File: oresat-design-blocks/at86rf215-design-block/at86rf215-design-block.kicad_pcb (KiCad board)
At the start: 2 copper layers, 1 part, among them U2 AT86RF215-ZU

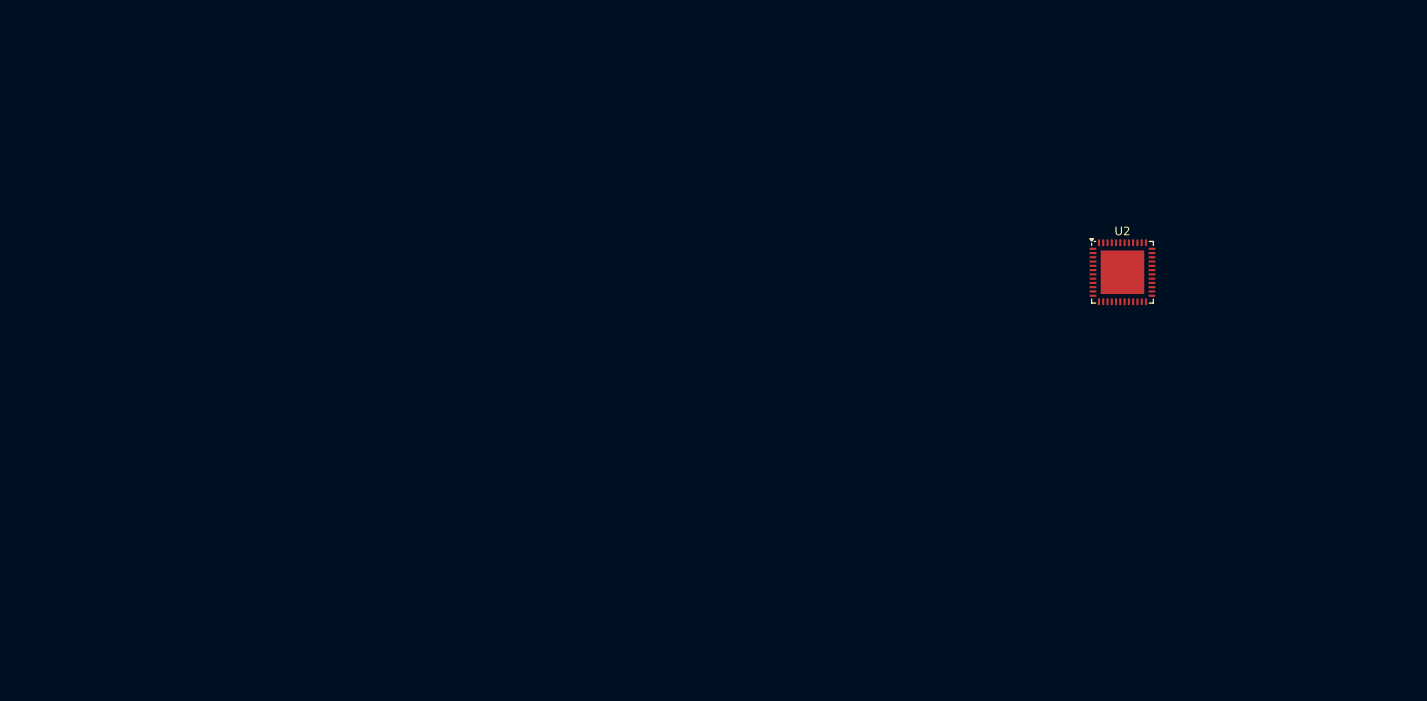
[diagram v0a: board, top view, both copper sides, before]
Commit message: added initial footprints and oreganized schematic. Started PCB
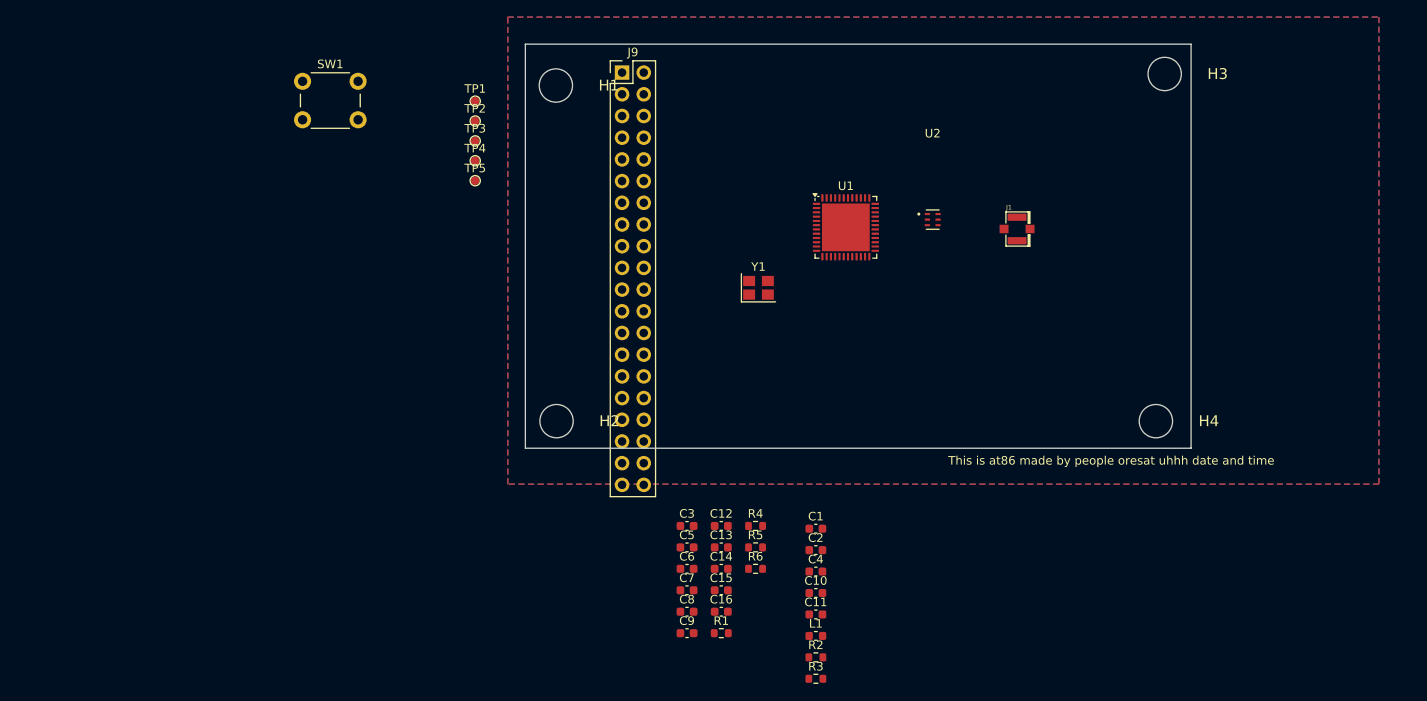
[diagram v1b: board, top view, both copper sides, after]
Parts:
- added C1: 1.8p, Capacitor_SMD:C_0603_1608Metric, F.Cu at (118.5, 113.1)
- added C10: 1.2p, Capacitor_SMD:C_0603_1608Metric, F.Cu at (118.5, 120.6)
- added C11: 1.2p, Capacitor_SMD:C_0603_1608Metric, F.Cu at (118.5, 123.1)
- added C12: 100 nF, Capacitor_SMD:C_0603_1608Metric, F.Cu at (107.4, 112.8)
- added C13: 100 nF, Capacitor_SMD:C_0603_1608Metric, F.Cu at (107.4, 115.3)
- added C14: 100 nF, Capacitor_SMD:C_0603_1608Metric, F.Cu at (107.4, 117.8)
- added C15: 100 nF, Capacitor_SMD:C_0603_1608Metric, F.Cu at (107.4, 120.3)
- added C16: 100 nF, Capacitor_SMD:C_0603_1608Metric, F.Cu at (107.4, 122.8)
- added C2: 1.8p, Capacitor_SMD:C_0603_1608Metric, F.Cu at (118.5, 115.6)
- added C3: 100n, Capacitor_SMD:C_0603_1608Metric, F.Cu at (103.4, 112.8)
- added C4: 0.8p, Capacitor_SMD:C_0603_1608Metric, F.Cu at (118.5, 118.1)
- added C5: 4.7n, Capacitor_SMD:C_0603_1608Metric, F.Cu at (103.4, 115.3)
- added C6: 2.2p, Capacitor_SMD:C_0603_1608Metric, F.Cu at (103.4, 117.8)
- added C7: 100 nF, Capacitor_SMD:C_0603_1608Metric, F.Cu at (103.4, 120.3)
- added C8: 100 nF, Capacitor_SMD:C_0603_1608Metric, F.Cu at (103.4, 122.8)
- added C9: 100 nF, Capacitor_SMD:C_0603_1608Metric, F.Cu at (103.4, 125.3)
- added H1: MountingHole, oresat-misc:M2-Press-Fit-Nut, F.Cu at (88.0, 61.2)
- added H2: MountingHole, oresat-misc:M2-Press-Fit-Nut, F.Cu at (88.1, 100.5)
- added H3: MountingHole, oresat-misc:M2-Press-Fit-Nut, F.Cu at (159.3, 59.9)
- added H4: MountingHole, oresat-misc:M2-Press-Fit-Nut, F.Cu at (158.3, 100.5)
- added J1: Conn_Coaxial, oresat-connectors:J-U.FL, F.Cu at (142.0, 78.0)
- added J9: Conn_02x20_Odd_Even, Connector_PinHeader_2.54mm:PinHeader_2x20_P2.54mm_Vertical, F.Cu at (95.8, 59.7)
- added L1: 5.6n, Inductor_SMD:L_0603_1608Metric, F.Cu at (118.5, 125.7)
- added R1: 100k, Resistor_SMD:R_0603_1608Metric, F.Cu at (107.4, 125.3)
- added R2: 0, Resistor_SMD:R_0603_1608Metric, F.Cu at (118.5, 128.2)
- added R3: 220, Resistor_SMD:R_0603_1608Metric, F.Cu at (118.5, 130.7)
- added R4: 39, Resistor_SMD:R_0603_1608Metric, F.Cu at (111.4, 112.8)
- added R5: 220, Resistor_SMD:R_0603_1608Metric, F.Cu at (111.4, 115.3)
- added R6: 100k, Resistor_SMD:R_0603_1608Metric, F.Cu at (111.4, 117.8)
- added SW1: RESET, Button_Switch_THT:SW_PUSH_6mm, F.Cu at (58.4, 60.7)
- added TP1: ~, oresat-misc:TestPoint_Pad_D1.0mm, F.Cu at (78.6, 63.1)
- added TP2: ~, oresat-misc:TestPoint_Pad_D1.0mm, F.Cu at (78.6, 65.4)
- added TP3: ~, oresat-misc:TestPoint_Pad_D1.0mm, F.Cu at (78.6, 67.7)
- added TP4: ~, oresat-misc:TestPoint_Pad_D1.0mm, F.Cu at (78.6, 70.0)
- added TP5: ~, oresat-misc:TestPoint_Pad_D1.0mm, F.Cu at (78.6, 72.4)
- added U1: AT86RF215, Package_DFN_QFN:QFN-48-1EP_7x7mm_P0.5mm_EP5.6x5.6mm, F.Cu at (122.0, 77.8)
- added Y1: TXETACSANF-26.000000, Crystal:Crystal_SMD_Abracon_ABM8AIG-4Pin_3.2x2.5mm, F.Cu at (111.8, 84.9)
- U2: value AT86RF215-ZU -> 2450FB15A050E; footprint Package_DFN_QFN:QFN-48-1EP_7x7mm_P0.5mm_EP5.1x5.1mm -> oresat-passives:2450FB15A050E_JOT
- moved U2 23.1 mm to (132.2, 76.9)
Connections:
- U2 pad 1: FEA24 -> Net-(U2-IN)
- U2 pad 2: FEB24 -> GND
- U2 pad 3: GNDA -> Net-(U2-OUT1)
- U2 pad 4: RFP24 -> Net-(U2-OUT2)
- U2 pad 5: RFN24 -> GND
- U2 pad 6: GNDA -> unconnected-(U2-NC-Pad6)
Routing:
- added copper zone on B.Cu, net GND
- added copper zone on F.Cu, net GND
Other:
- board outline added: 77.9 x 47.3 mm
- board text added: "This is at86 made by people oresat uhhh date and time"

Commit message: added initial 436.5mhz circuit
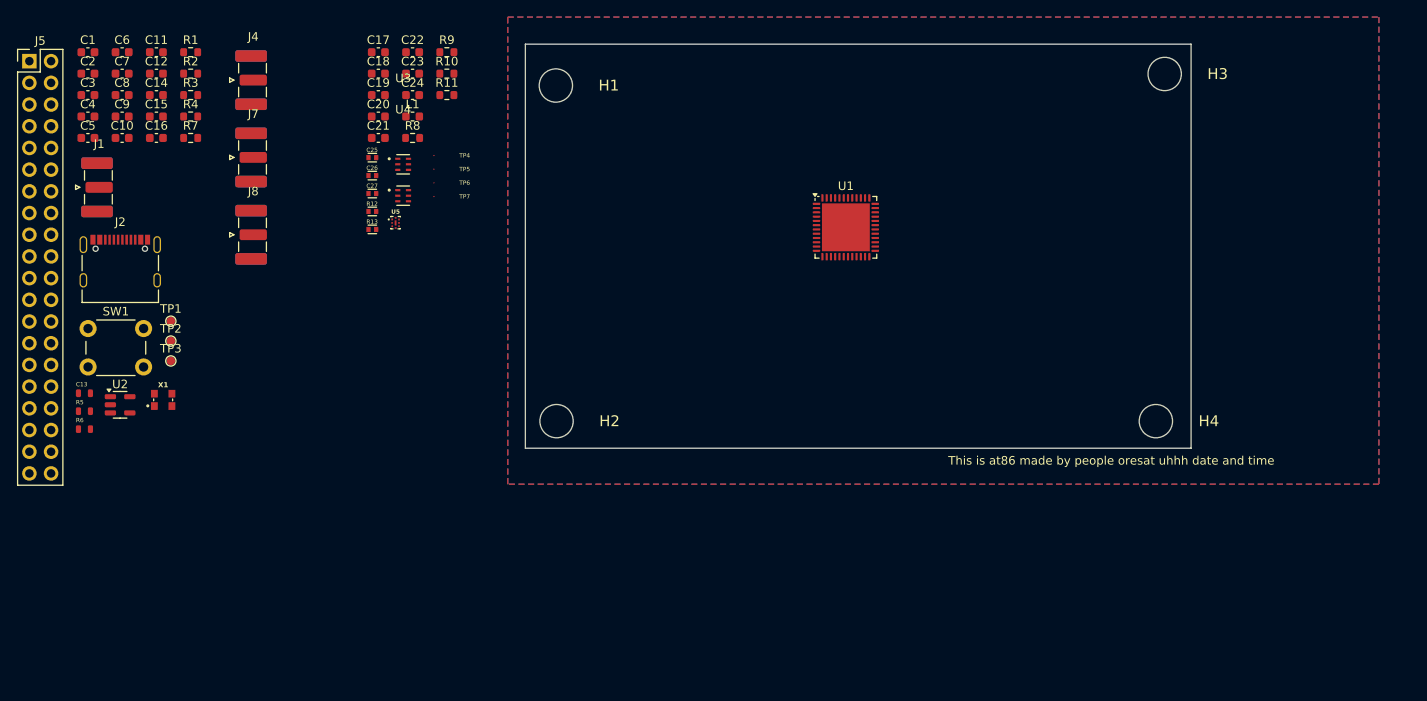
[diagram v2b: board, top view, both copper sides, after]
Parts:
- removed J9: Conn_02x20_Odd_Even, Connector_PinHeader_2.54mm:PinHeader_2x20_P2.54mm_Vertical
- removed Y1: TXETACSANF-26.000000, Crystal:Crystal_SMD_Abracon_ABM8AIG-4Pin_3.2x2.5mm
- added C17: 1.8p, Capacitor_SMD:C_0603_1608Metric, F.Cu at (67.3, 57.3)
- added C18: 1.8p, Capacitor_SMD:C_0603_1608Metric, F.Cu at (67.3, 59.8)
- added C19: 0.8p, Capacitor_SMD:C_0603_1608Metric, F.Cu at (67.3, 62.3)
- added C20: 15p, Capacitor_SMD:C_0603_1608Metric, F.Cu at (67.3, 64.8)
- added C21: 1.2p, Capacitor_SMD:C_0603_1608Metric, F.Cu at (67.3, 67.4)
- added C22: 2.2p, Capacitor_SMD:C_0603_1608Metric, F.Cu at (71.3, 57.3)
- added C23: 1.2p, Capacitor_SMD:C_0603_1608Metric, F.Cu at (71.3, 59.8)
- added C24: 2.2p, Capacitor_SMD:C_0603_1608Metric, F.Cu at (71.3, 62.3)
- added C25: 100p, oresat-passives:0402-C, F.Cu at (66.6, 69.7)
- added C26: 2200p, oresat-passives:0402-C, F.Cu at (66.6, 71.8)
- added C27: 100p, oresat-passives:0402-C, F.Cu at (66.6, 73.9)
- added J2: USB4105-GF-A, Connector_USB:USB_C_Receptacle_Palconn_UTC16-G, F.Cu at (37.0, 81.8)
- added J4: SMA, Connector_Coaxial:SMA_Samtec_SMA-J-P-H-ST-EM1_EdgeMount, F.Cu at (52.6, 60.6)
- added J5: Conn_02x20_Odd_Even, Connector_PinHeader_2.54mm:PinHeader_2x20_P2.54mm_Vertical, F.Cu at (26.4, 58.4)
- added J7: SMA, Connector_Coaxial:SMA_Samtec_SMA-J-P-H-ST-EM1_EdgeMount, F.Cu at (52.6, 69.6)
- added J8: SMA, Connector_Coaxial:SMA_Samtec_SMA-J-P-H-ST-EM1_EdgeMount, F.Cu at (52.6, 78.7)
- added R10: 10k, Resistor_SMD:R_0603_1608Metric, F.Cu at (75.3, 59.8)
- added R11: 10k, Resistor_SMD:R_0603_1608Metric, F.Cu at (75.3, 62.3)
- added R12: 10k, oresat-passives:0402-C, F.Cu at (66.6, 76.0)
- added R13: 5.62k, oresat-passives:0402-C, F.Cu at (66.6, 78.1)
- added R7: 100k, Resistor_SMD:R_0603_1608Metric, F.Cu at (45.3, 67.4)
- added R8: 0, Resistor_SMD:R_0603_1608Metric, F.Cu at (71.3, 67.4)
- added R9: 0, Resistor_SMD:R_0603_1608Metric, F.Cu at (75.3, 57.3)
- added TP6: ~, oresat-misc:TestPoint_RF_Probe, F.Cu at (73.8, 72.6)
- added TP7: ~, oresat-misc:TestPoint_RF_Probe, F.Cu at (73.8, 74.2)
- added U3: 2450FB15A050E, oresat-passives:2450FB15A050E_JOT, F.Cu at (70.2, 70.4)
- added U4: NCS2-62+, oresat-passives:2450FB15A050E_JOT, F.Cu at (70.2, 74.1)
- added U5: QPC1022, oresat-ics:QPC1022, F.Cu at (69.3, 77.3)
- added X1: TXETALSANF-26.000000, oresat-ics:X_TCXO_SMD_Taitien_2.5x2.0mm, F.Cu at (42.1, 98.0)
- C1: value 1.8p -> 100n
- C10, C11: value 1.2p -> 100 nF
- C13: value 100 nF -> 100n; footprint Capacitor_SMD:C_0603_1608Metric -> oresat-passives:0603-C-NOSILK
- C14: value 100 nF -> 4.7u
- C15: value 100 nF -> 10n
- C16: value 100 nF -> 1u
- C2: value 1.8p -> 4.7n
- C3: value 100n -> 1n
- C4: value 0.8p -> 2.2p
- C5: value 4.7n -> 100 nF
- C6: value 2.2p -> 100 nF
- J1: value Conn_Coaxial -> SMA; footprint oresat-connectors:J-U.FL -> Connector_Coaxial:SMA_Samtec_SMA-J-P-H-ST-EM1_EdgeMount
- R2: value 0 -> 39
- R4: value 39 -> 100k
- R5: value 220 -> 5.1k; footprint Resistor_SMD:R_0603_1608Metric -> oresat-passives:0603-C-NOSILK
- R6: value 100k -> 5.1k; footprint Resistor_SMD:R_0603_1608Metric -> oresat-passives:0603-C-NOSILK
- TP4, TP5: footprint oresat-misc:TestPoint_Pad_D1.0mm -> oresat-misc:TestPoint_RF_Probe
- U2: value 2450FB15A050E -> LP2985AIM5-1.8_NOPB; footprint oresat-passives:2450FB15A050E_JOT -> Package_TO_SOT_SMD:SOT-23-5
- moved J1 107.6 mm to (34.6, 73.1)
- moved C1 101.8 mm to (33.3, 57.3)
- moved C2 101.8 mm to (33.3, 59.8)
- moved C11 101.4 mm to (41.3, 57.3)
- moved C4 100.5 mm to (33.3, 64.8)
- moved R2 100.1 mm to (45.3, 59.8)
- moved R3 100.1 mm to (45.3, 62.3)
- moved U2 97.6 mm to (37.0, 98.6)
- moved C10 97.1 mm to (37.3, 67.4)
- moved R1 92.1 mm to (45.3, 57.3)
- moved C7 89.6 mm to (37.3, 59.8)
- moved C9 89.6 mm to (37.3, 64.8)
- moved C6 89.6 mm to (37.3, 57.3)
- moved C8 89.6 mm to (37.3, 62.3)
- moved C3 86.4 mm to (33.3, 62.3)
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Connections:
- C1 pad 1: Net-(U2-OUT1) -> GND
- C1 pad 2: RFN24 -> +3V3
- C10 pad 1: Net-(C10-Pad1) -> Net-(U1-AVDD0)
- C11 pad 1: Net-(J1-In) -> +3V3
- C12 pad 1: +3V3 -> Net-(U1-AVDD1)
- C13 pad 1: +3V3 -> GND
- C13 pad 2: GND -> Net-(J2-SHIELD)
- C14 pad 1: +3V3 -> 5V
- C15 pad 1: +3V3 -> Net-(U2-BYPASS)
- C16 pad 1: +3V3 -> 3.3V
- C2 pad 1: RFP24 -> ~{RSTN}
- C2 pad 2: Net-(U2-OUT2) -> GND
- C3 pad 1: GND -> Net-(U1-TXCO)
- C3 pad 2: +3V3 -> Net-(X1-OUT)
- C4 pad 1: Net-(C10-Pad1) -> GND
- C4 pad 2: Net-(U2-IN) -> CLKO
- C5 pad 1: ~{RSTN} -> +3V3
- C6 pad 1: GND -> +3V3
- C6 pad 2: CLKO -> GND
- C7 pad 1: DVDD -> +3V3
- C8 pad 1: AVDD1 -> +3V3
- C9 pad 1: AVDD0 -> Net-(U1-DVDD)
- L1 pad 1: Net-(U2-OUT1) -> Net-(U3-OUT1)
- L1 pad 2: Net-(U2-OUT2) -> Net-(U3-OUT2)
- R2 pad 1: Net-(C10-Pad1) -> ~{RSTN}
- R2 pad 2: Net-(J1-In) -> Net-(R2-Pad2)
- R3 pad 1: Net-(J1-In) -> Net-(U1-CLKO)
- R3 pad 2: GND -> CLKO
- R4 pad 1: ~{RSTN} -> Net-(U1-XTAL2)
- R4 pad 2: Net-(R4-Pad2) -> GND
- R5 pad 1: Net-(U1-CLKO) -> Net-(J2-CC2)
- R5 pad 2: CLKO -> GND
- R6 pad 1: Net-(U1-XTAL2) -> Net-(J2-CC1)
- SW1 pad 1: Net-(R4-Pad2) -> Net-(R2-Pad2)
- TP1 pad 1: Net-(R4-Pad2) -> Net-(R2-Pad2)
- TP2 pad 1: CLKO -> Net-(J2-D--PadA7)
- TP3 pad 1: AVDD0 -> Net-(J2-D+-PadA6)
- TP4 pad 1: AVDD1 -> Net-(U3-IN)
- TP5 pad 1: DVDD -> Net-(U4-IN)
- U1 pad 14: AVDD0 -> Net-(U1-AVDD0)
- U1 pad 37: DVDD -> Net-(U1-DVDD)
- U1 pad 47: AVDD1 -> Net-(U1-AVDD1)
- U2 pad 1: Net-(U2-IN) -> 3.3V
- U2 pad 3: Net-(U2-OUT1) -> Net-(U2-EN)
- U2 pad 4: Net-(U2-OUT2) -> Net-(U2-BYPASS)
- U2 pad 5: GND -> 5V

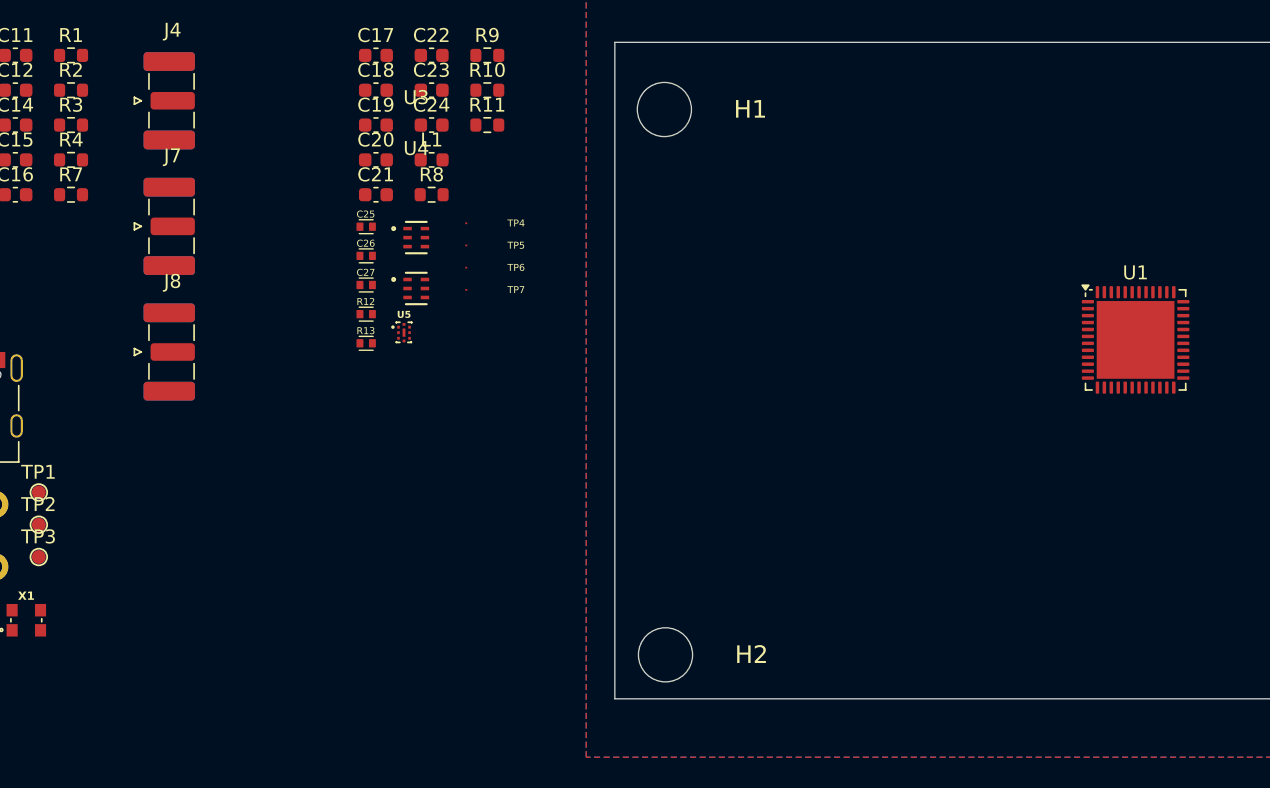
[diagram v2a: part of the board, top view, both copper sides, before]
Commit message: Design review and cleanup of AT86RF215 eval board; ready for layout.
Added footprints to SMAs, made a symbol for a balun, cleaned up and renamed schematic. Added terminal block for power just cause.
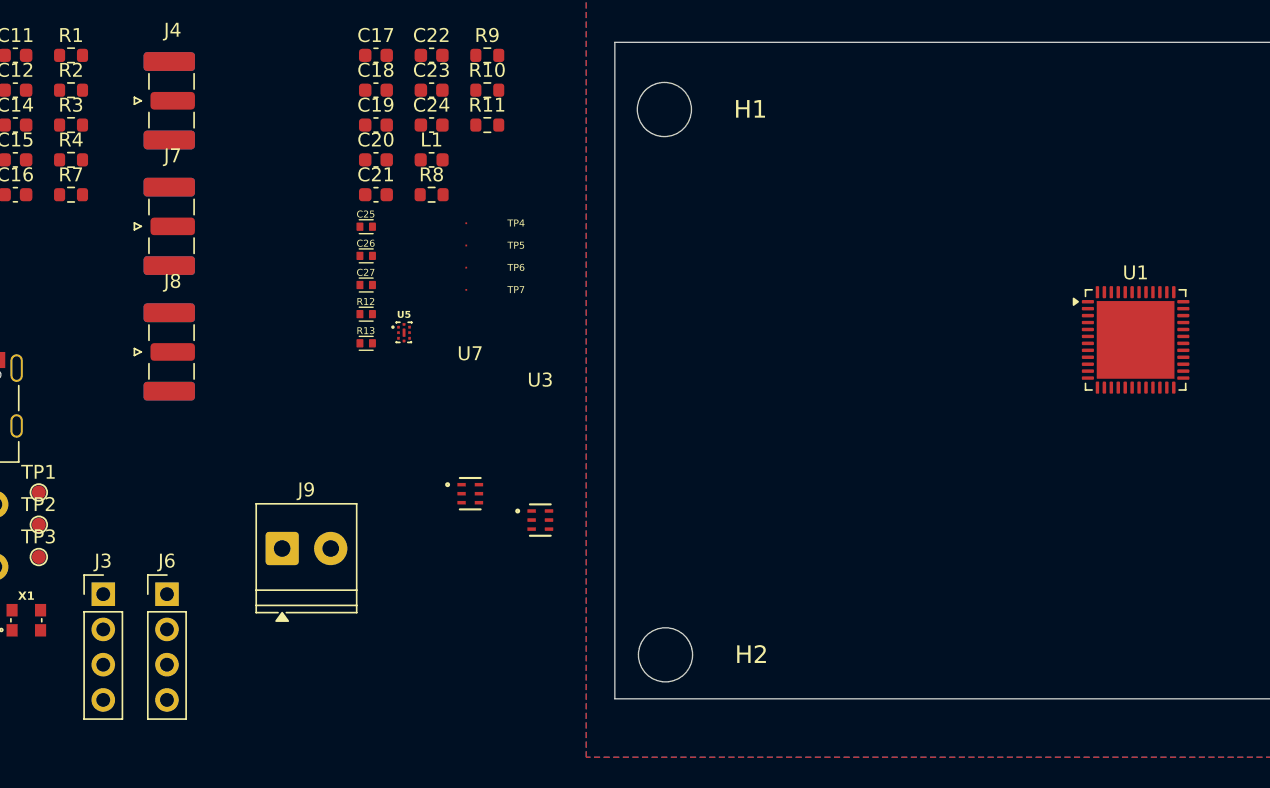
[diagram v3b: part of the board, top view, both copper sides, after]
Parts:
- removed U4: NCS2-62+, oresat-passives:2450FB15A050E_JOT
- added J3: Conn_01x04, Connector_PinHeader_2.54mm:PinHeader_1x04_P2.54mm_Vertical, F.Cu at (47.6, 96.1)
- added J6: Conn_01x04, Connector_PinHeader_2.54mm:PinHeader_1x04_P2.54mm_Vertical, F.Cu at (52.2, 96.1)
- added J9: Screw_Terminal_01x02, TerminalBlock_Phoenix:TerminalBlock_Phoenix_PT-1,5-2-3.5-H_1x02_P3.50mm_Horizontal, F.Cu at (60.5, 92.8)
- added U7: NCS2-62+, oresat-passives:2450FB15A050E_JOT, F.Cu at (74.0, 88.9)
- moved U3 22.2 mm to (79.1, 90.8)
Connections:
- J1 pad 1: (no net) -> CLKO
- J1 pad 2: (no net) -> GND
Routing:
- added copper zone on In1.Cu, net GND
- added copper zone on In2.Cu, net GND
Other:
- copper layers 2 -> 4

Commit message: started component layout and initial routing on PCB
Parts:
- removed H1, H2, H3, H4: MountingHole, oresat-misc:M2-Press-Fit-Nut
- removed J3, J6: Conn_01x04, Connector_PinHeader_2.54mm:PinHeader_1x04_P2.54mm_Vertical
- removed J5: Conn_02x20_Odd_Even, Connector_PinHeader_2.54mm:PinHeader_2x20_P2.54mm_Vertical
- C3: footprint Capacitor_SMD:C_0603_1608Metric -> Capacitor_SMD:C_0402_1005Metric
- moved J4 103.4 mm to (152.2, 88.3)
- moved J7 100.1 mm to (152.2, 80.0)
- moved J8 99.8 mm to (152.2, 71.6)
- moved SW1 97.7 mm to (126.0, 58.8)
- moved C2 92.4 mm to (124.2, 76.7), turned to 90 degrees
- moved C1 91.1 mm to (123.1, 72.3), turned to -90 degrees
- moved C6 89.0 mm to (121.1, 87.3), turned to -90 degrees
- moved C3 87.6 mm to (119.8, 75.8), turned to 90 degrees
- moved C5 86.6 mm to (117.6, 87.3), turned to -90 degrees
- moved C12 86.3 mm to (123.3, 86.6)
- moved C10 85.7 mm to (122.6, 75.4), turned to 90 degrees
- moved C8 84.8 mm to (121.1, 75.6), turned to 90 degrees
- moved TP1 84.2 mm to (121.6, 58.8), turned to 90 degrees
- moved X1 82.8 mm to (120.8, 72.4), turned to 180 degrees
- moved R1 82.8 mm to (125.8, 76.6), turned to 90 degrees
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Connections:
- net 5V renamed +5V
- C1 pad 2: +3V3 -> +3.3V
- C11 pad 1: +3V3 -> +3.3V
- C16 pad 1: 3.3V -> +3.3V
- C5 pad 1: +3V3 -> +3.3V
- C6 pad 1: +3V3 -> +3.3V
- C7 pad 1: +3V3 -> +3.3V
- C8 pad 1: +3V3 -> +3.3V
- R1 pad 2: +3V3 -> +3.3V
- R7 pad 1: 3.3V -> +3.3V
- U1 pad 15: +3V3 -> +3.3V
- U1 pad 21: +3V3 -> +3.3V
- U1 pad 29: +3V3 -> +3.3V
- U1 pad 39: +3V3 -> +3.3V
- U1 pad 46: +3V3 -> +3.3V
- U2 pad 1: 3.3V -> +3.3V
- X1 pad 4: +3V3 -> +3.3V
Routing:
- net Net-(J2-SHIELD): track 0.00 -> 19.4 mm
- net +3.3V: track 0.00 -> 16.1 mm, vias 0 -> 9
- net Net-(J2-D+-PadA6): track 0.00 -> 10.6 mm
- net Net-(J2-D--PadA7): track 0.00 -> 10.3 mm
- net Net-(R2-Pad2): track 0.00 -> 9.01 mm
- net Net-(U1-XTAL2): track 0.00 -> 5.02 mm
- net ~{RSTN}: track 0.00 -> 3.93 mm
- net RFP24: track 0.00 -> 3.03 mm
- net RFN24: track 0.00 -> 2.58 mm
- net Net-(U1-AVDD0): track 0.00 -> 2.49 mm
- net Net-(U1-AVDD1): track 0.00 -> 2.49 mm
- net Net-(X1-OUT): track 0.00 -> 2.19 mm
- net Net-(U2-EN): track 0.00 -> 2.01 mm
- net +5V: track 0.00 -> 1.99 mm
- net Net-(J2-CC1): track 0.00 -> 1.98 mm
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- added copper zone on In2.Cu, net +3.3V
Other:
- board size 77.9 x 47.3 mm -> 69.4 x 52.5 mm
